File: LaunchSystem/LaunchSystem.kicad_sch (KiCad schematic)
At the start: 23 parts, among them J1 GND - Ignition, J10 GND - Ignition, J2 VCC - +9V - Ignition, J5 VCC - 9V IN - ESP, J6 VCC - 9V IN - Ignition, J7 VCC - 9V IN - Ignition, J8 GND - Ignition, J9 GND - ESP, K1 43.41.7.005.2000, Q1 BC547, SW1 SW_SPDT, U2 L7805

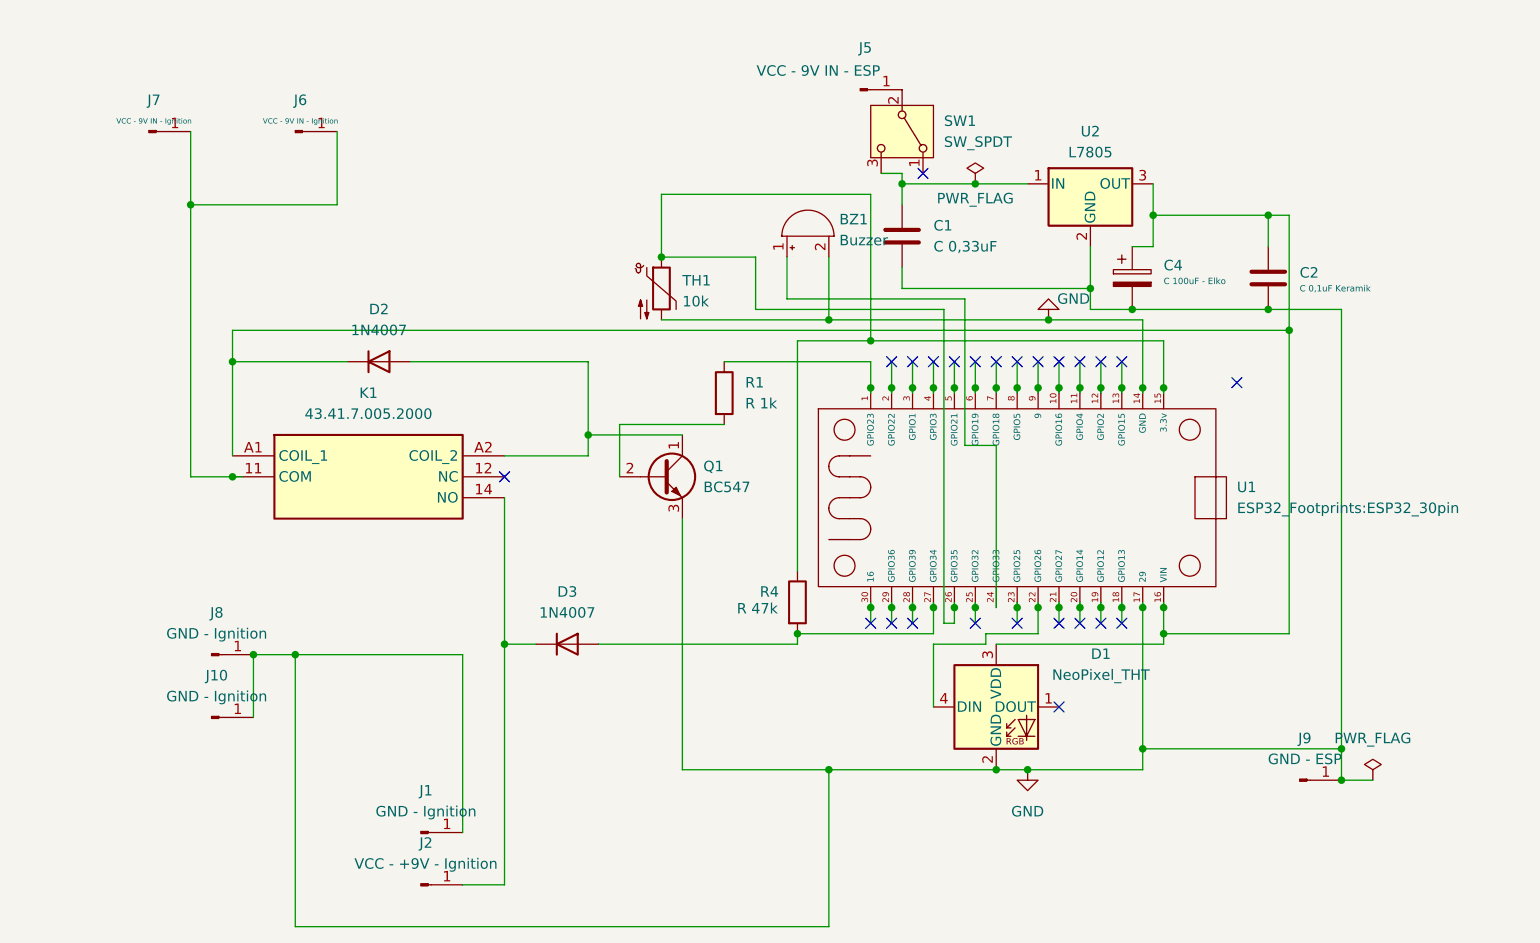
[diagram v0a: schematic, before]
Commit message: Update KiCad PWR section, footprints & nets
Add KiCad lock/history ignores to .gitignore. Major PCB changes: rename nets (GPIO35 -> 3.3v), add axial resistor footprint, replace/update TO-220 footprint for L7805 and update related pads/traces/zones. Schematic updates: bump sch revision to V3, add title block/date/rev/company, reposition components/junctions/wires, add PWR section label and a resistor symbol (R2), move PWR_FLAG and connectors. Overall: layout cleanup, footprint corrections and schematic revision to reflect PWR section rework.
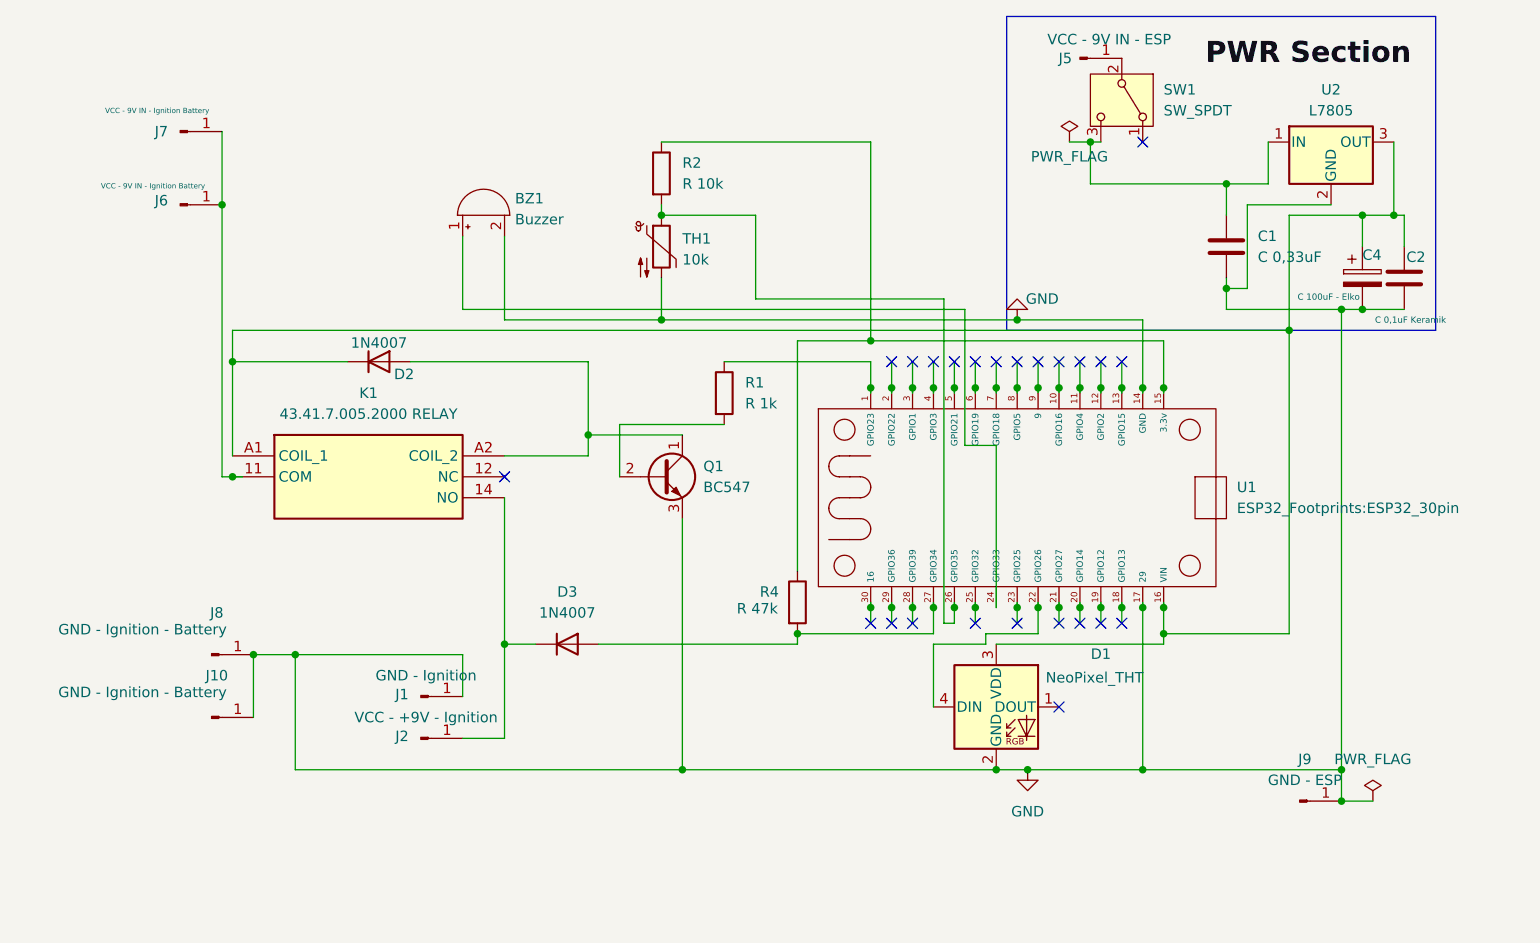
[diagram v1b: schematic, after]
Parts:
- added R2: R 10k, Resistor_THT:R_Axial_DIN0207_L6.3mm_D2.5mm_P7.62mm_Horizontal, symbol Device:R
- J10, J8: value GND - Ignition -> GND - Ignition - Battery
- J6, J7: value VCC - 9V IN - Ignition -> VCC - 9V IN - Ignition Battery
- K1: value 43.41.7.005.2000 -> 43.41.7.005.2000 RELAY
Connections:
- net at R4.1, U1.15 (3.3v): now also R2.1; no longer TH1.1, U1.26 (GPIO35)
- new net: R2.2, TH1.1, U1.26 (GPIO35)
- no-connect marks 25 -> 24
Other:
- company: (none) -> NeoLabs-Rockets
- title: (none) -> LaunchSystem
- moved on the sheet: BZ1, C1, C2, C4, J1, J2, J5, J6, J7, J9, SW1, TH1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
